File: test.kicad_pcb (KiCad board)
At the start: 2 copper layers, 86 parts, among them U2 Raspberry_Pi_Pico

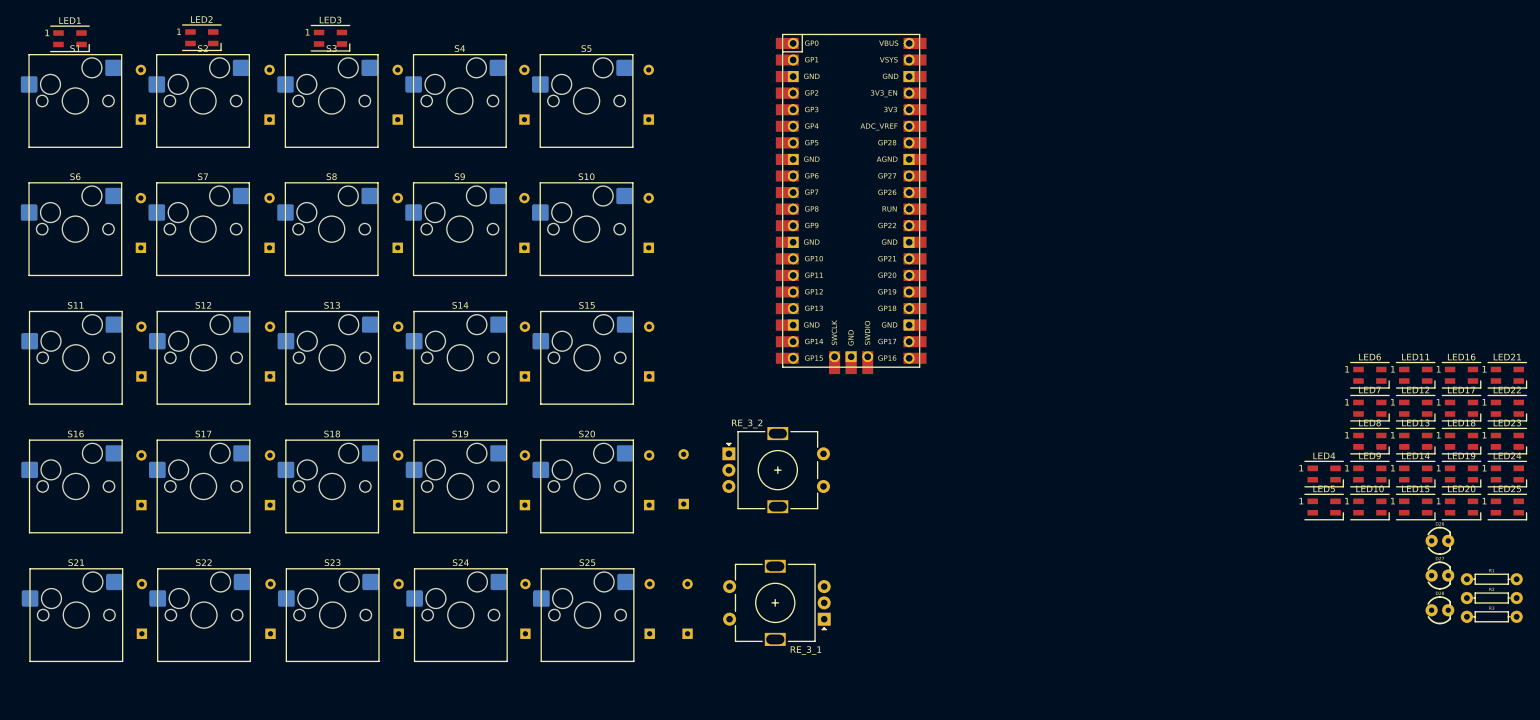
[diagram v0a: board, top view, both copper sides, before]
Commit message: Arrange PCB to 5x5 button layout and 2 rotary encoder
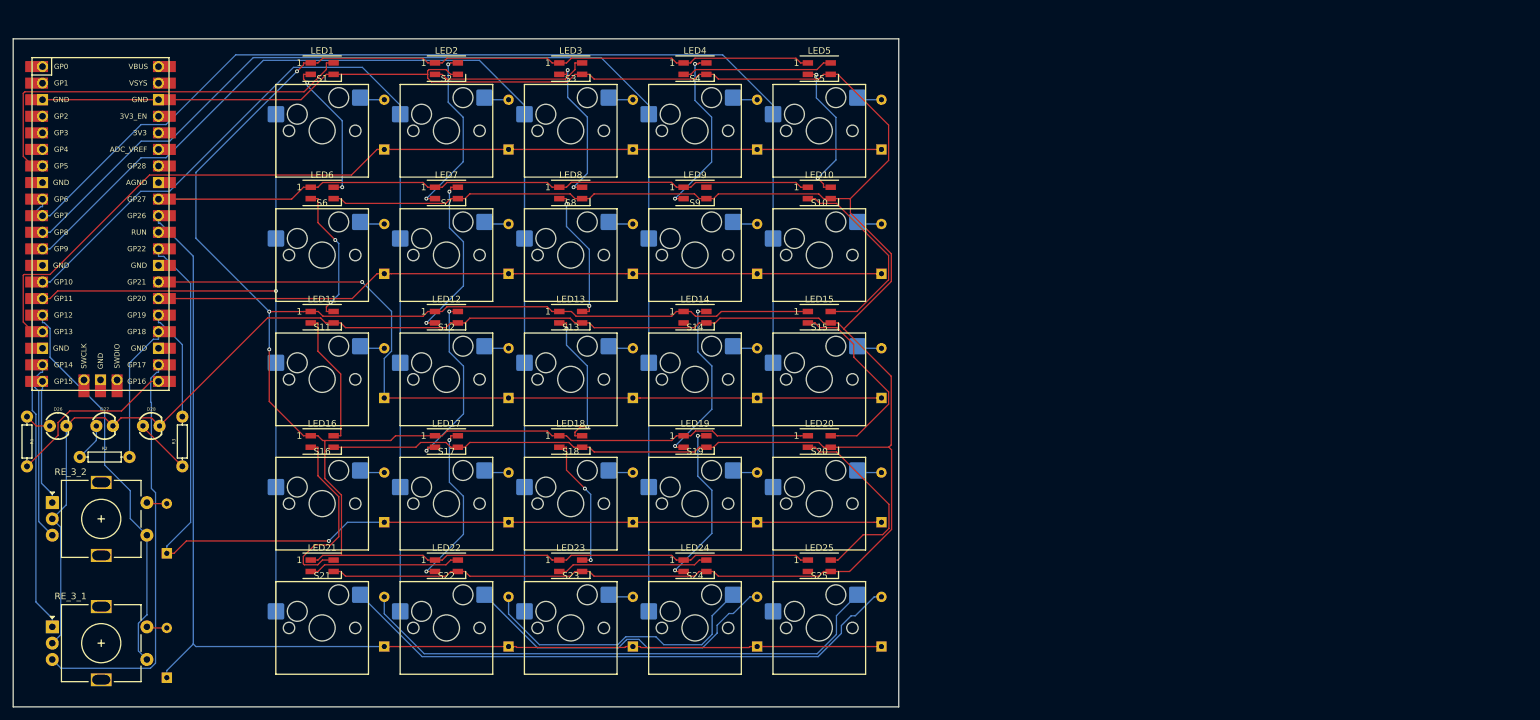
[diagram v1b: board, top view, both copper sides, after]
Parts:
- moved R1 225.5 mm to (18.2, 77.0), turned to -90 degrees
- moved R2 213.7 mm to (30.1, 79.4)
- moved D26 212.5 mm to (23.0, 74.6)
- moved D27 205.9 mm to (30.1, 74.6)
- moved R3 202.5 mm to (42.0, 77.0), turned to 90 degrees
- moved D28 199.5 mm to (37.3, 74.6)
- moved LED21 184.0 mm to (63.5, 96.1)
- moved LED16 174.9 mm to (63.5, 77.0)
- moved LED11 167.9 mm to (63.5, 58.0)
- moved LED22 164.4 mm to (82.5, 96.1)
- moved LED6 163.0 mm to (63.5, 38.9)
- moved LED17 155.7 mm to (82.5, 77.0)
- moved LED12 149.2 mm to (82.5, 58.0)
- moved LED7 145.3 mm to (82.5, 38.9)
- moved LED23 144.8 mm to (101.6, 96.1)
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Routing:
- net GND: track 0.00 -> 642.2 mm
- net VCC: track 0.00 -> 521.0 mm, vias 0 -> 3
- net Column 5: track 0.00 -> 203.0 mm
- net Column 4: track 0.00 -> 184.6 mm
- net Row 4: track 0.00 -> 180.7 mm
- net Column 3: track 0.00 -> 166.3 mm
- net Row 3: track 0.00 -> 162.2 mm, vias 0 -> 1
- net Row 0: track 0.00 -> 150.3 mm
- net Column 2: track 0.00 -> 148.4 mm
- net Row 2: track 0.00 -> 127.5 mm, vias 0 -> 1
- net Column 1: track 0.00 -> 112.5 mm, vias 0 -> 1
- net Row 1: track 0.00 -> 112.4 mm
- net Net-(D21-A): track 0.00 -> 88.3 mm
- net Net-(D25-A): track 0.00 -> 83.1 mm
- net /ENCODER0_L1: track 0.00 -> 67.6 mm
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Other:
- board outline added: 135.7 x 102.4 mm

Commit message: Update layout to mimic normal NumPad
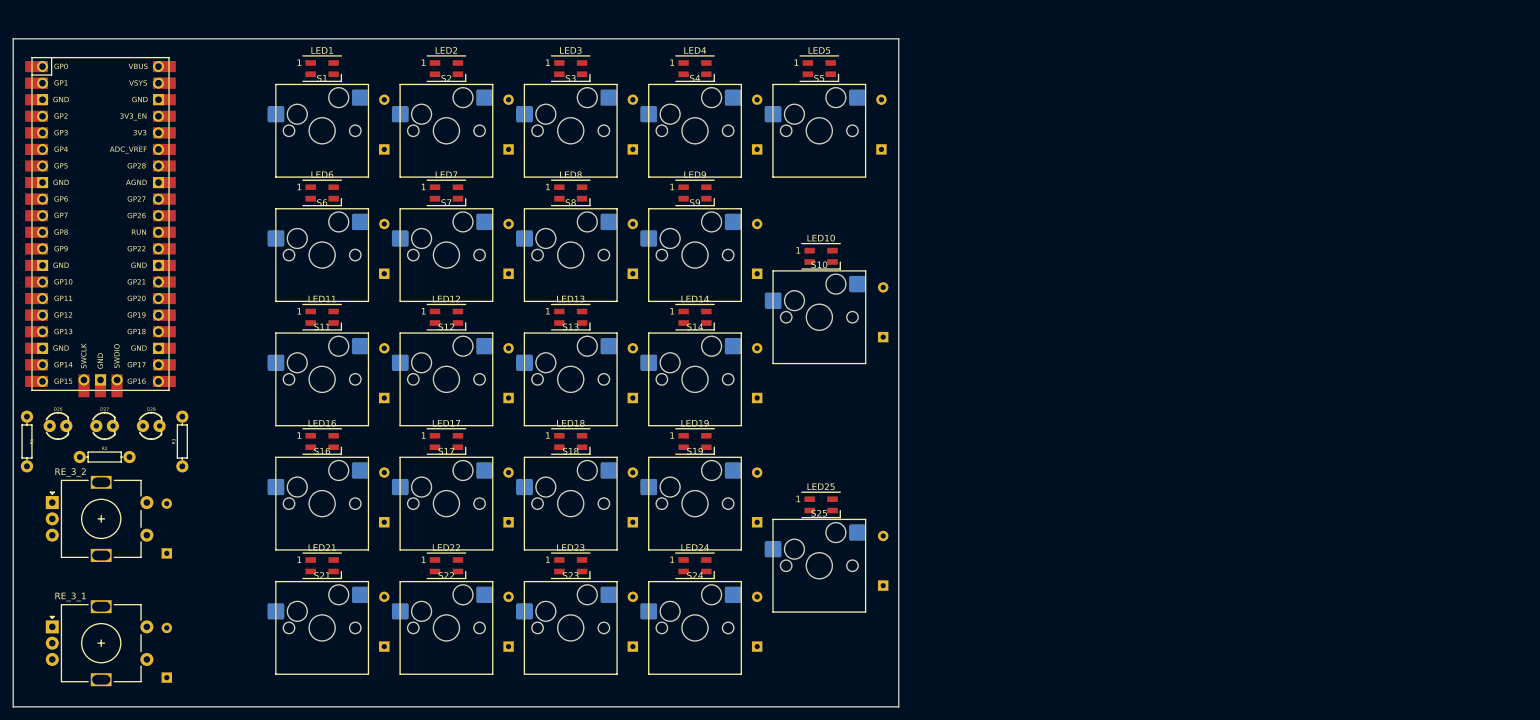
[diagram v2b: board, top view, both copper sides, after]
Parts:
- removed D15, D20: Diode, ScottoKeebs_Components:Diode_DO-35
- removed LED15, LED20: SK6812MINI, LED_SMD:LED_SK6812MINI_PLCC4_3.5x3.5mm_P1.75mm
- removed S15, S20: Keyswitch, ScottoKeebs_Hotswap:Hotswap_MX_1.00u
- S10, S25: footprint ScottoKeebs_Hotswap:Hotswap_MX_1.00u -> ScottoKeebs_Hotswap:Hotswap_MX_2.00u_90deg
- moved D10 9.72 mm to (149.5, 61.0)
- moved LED10 9.72 mm to (139.9, 48.6)
- moved S25 9.53 mm to (139.7, 96.1)
- moved S10 9.53 mm to (139.7, 58.0)
- moved D21 9.34 mm to (149.5, 99.1)
- moved LED25 9.34 mm to (139.9, 86.7)
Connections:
- LED25 pad 4: Net-(LED20-DOUT) -> Net-(LED10-DOUT)
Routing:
- net GND: track 642.2 -> 0.00 mm
- net VCC: track 521.0 -> 0.00 mm, vias 3 -> 0
- net Column 5: track 203.0 -> 0.00 mm
- net Column 4: track 184.6 -> 0.00 mm
- net Row 4: track 180.7 -> 0.00 mm
- net Column 3: track 166.3 -> 0.00 mm
- net Row 3: track 162.2 -> 0.00 mm, vias 1 -> 0
- net Row 0: track 150.3 -> 0.00 mm
- net Column 2: track 148.4 -> 0.00 mm
- net Row 2: track 127.5 -> 0.00 mm, vias 1 -> 0
- net Column 1: track 112.5 -> 0.00 mm, vias 1 -> 0
- net Row 1: track 112.4 -> 0.00 mm
- net Net-(D21-A): track 88.3 -> 0.00 mm
- net Net-(D25-A): track 83.1 -> 0.00 mm
- net /ENCODER0_L1: track 67.6 -> 0.00 mm
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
